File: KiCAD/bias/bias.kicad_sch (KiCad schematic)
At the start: 67 parts, among them J1 Conn_Coaxial_Small, J11 GRID_BIAS, J2 Conn_Coaxial_Small, J3 Screw_Terminal_01x02, J4 Conn_Coaxial_Small, J5 Screw_Terminal_01x02, J6 Conn_Coaxial_Small, J7 Screw_Terminal_01x02, J8 Screw_Terminal_01x02, J9 Conn_Coaxial_Small, Q2 2N7000, Q3 2N7000, U10 OPA454, U11 LM4040LP-5, U12 LM393, U13 OPA1641, U14 OPA1641, U5 OPA454, U9 LM7805_TO220

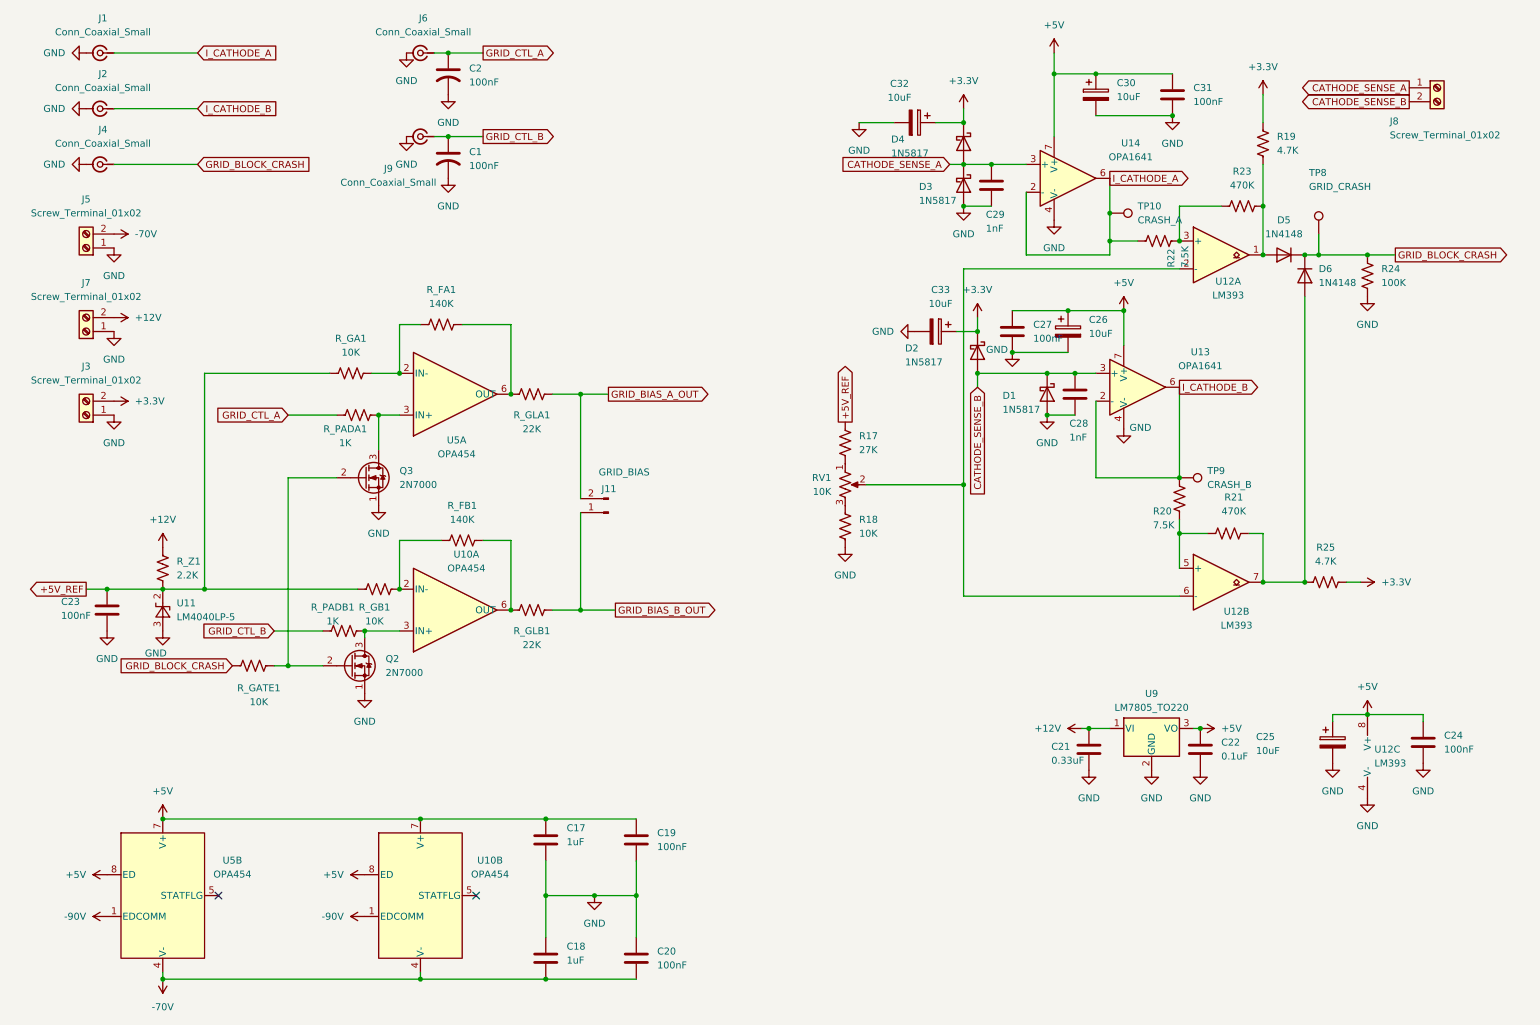
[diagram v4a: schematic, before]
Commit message: KiCad revB: schematic review pass — I2C, ENC_INT, GND returns, GRID_BLOCK_CRASH clamp
Result of extended review pass against fresh netlists across all four
boards. All connectivity blockers resolved.

- Si5351 SDA/SCL wired via 0R jumpers (R8/R9) puts I2C on PCB traces
  for PCF8575 U17 and the RJ45 to the front panel. MCP4728 side has
  parallel 0R jumpers (R3/R4/R5) left DNP by default — STEMMA-QT is
  the intended path.
- ENC_INT chain unified end-to-end with staged names:
  ENC_INT_RAW (frontpanel encoder wire-OR) → ENC_INT_CLEAN (across
  CAT + analog pass-through) → ENC_INT_FINAL (post-protoshield
  conditioning). Frontpanel U4 (MCP1700-3.3 LDO) sources the +3.3V
  the pull-up R4 needs; pull-up moved to encoder side for sharper
  falling edges over the 2 m CAT run.
- Protoshield GRID_BLOCK_CRASH gets 1N4728A Zener clamp (D5),
  matching the I_CATHODE and MBL600 5V→3.3V clamp topology.
- Protoshield MBL600 conditioning rebuilt: 1K series + 100nF filter
  + 1N4728A clamp (was 10K/20K divider + 22pF that filtered nothing
  below RF).
- PADDLE_A/B and RESET_N removed from analog board — case-mounted
  switches wire directly to protoshield.
- Protoshield J1/J6 widened to 3-pin to include GND returns for the
  case-mounted paddle and reset switches.
- Bias board reference designators reorganized functionally
  (R_FA/R_FB feedback, R_GA/R_GB gain, R_PADA/R_PADB, R_GLA/R_GLB
  grid line, R_GATE, R_Z).
- New Documentation/control_board_functional_blocks.md captures
  KeyUp/Gate 2 keying, relay assignments (J6=T/R, J7=HV primary,
  J8=HV inrush), CD14538B heartbeat watchdog, TR_SENSE interlock,
  and J13 power-migration header.
- Fresh netlists exported for all four boards.

Co-Authored-By: Claude Opus 4.7 <noreply@anthropic.com>
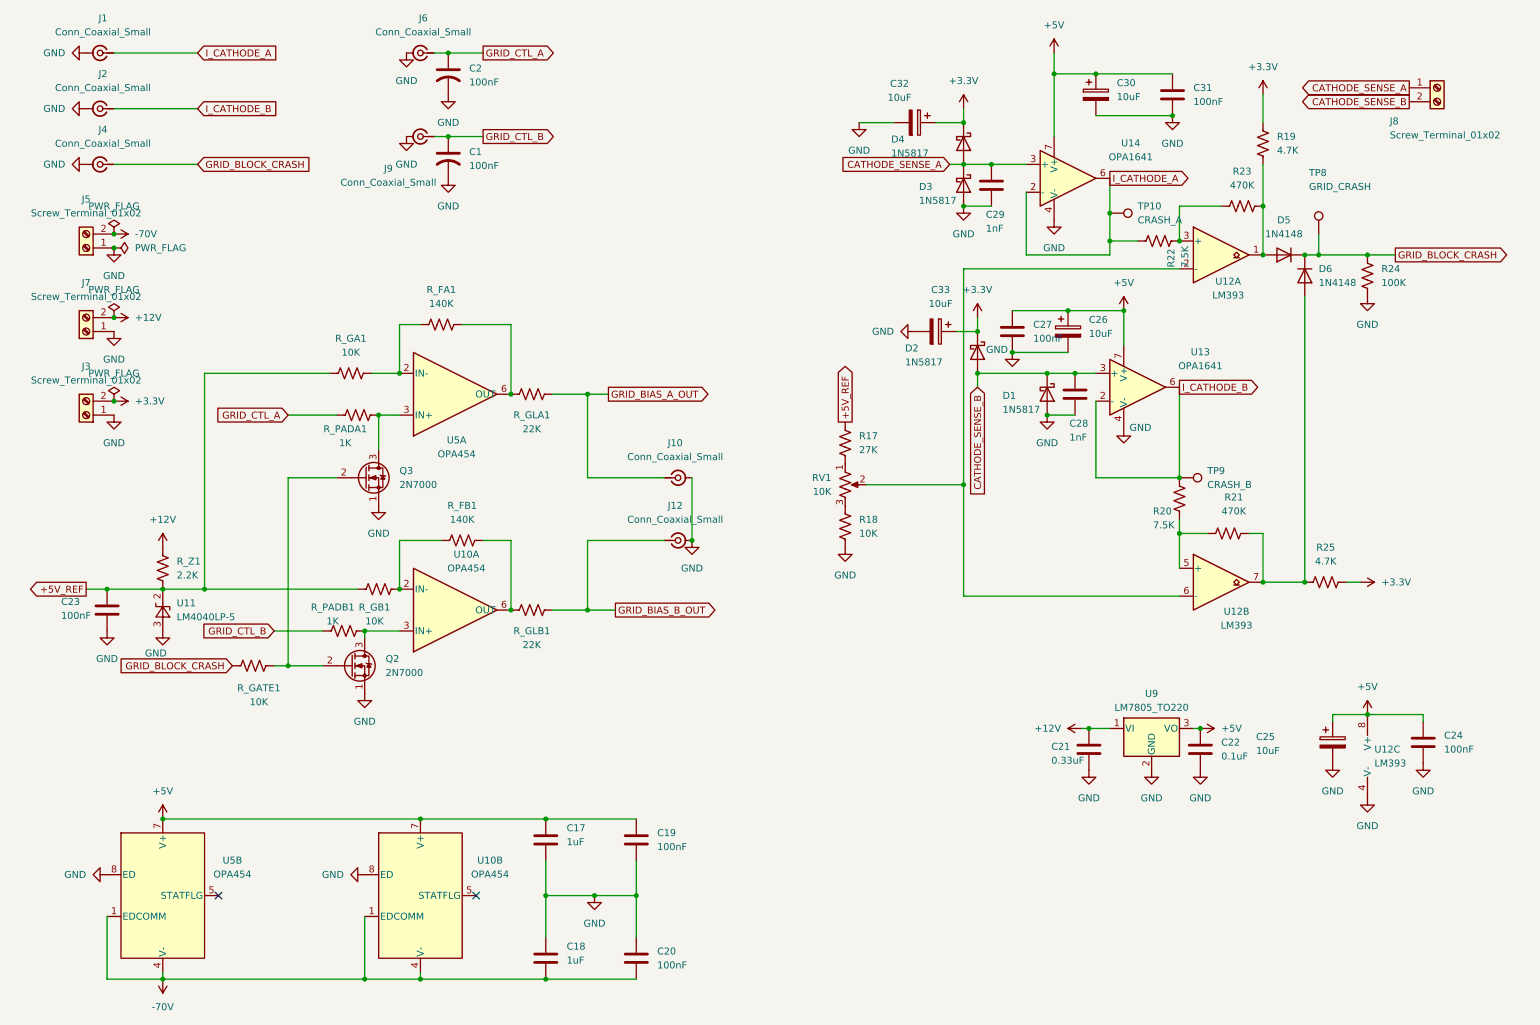
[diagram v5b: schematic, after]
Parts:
- removed J11: GRID_BIAS, Connector_PinHeader_2.54mm:PinHeader_1x02_P2.54mm_Vertical, symbol Connector:Conn_01x02_Pin
- added J10, J12: Conn_Coaxial_Small, symbol Connector:Conn_Coaxial_Small
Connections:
- net -90V is gone; now on net -70V: U10.1 (EDCOMM), U5.1 (EDCOMM)
- net +5V: no longer U10.8 (ED), U5.8 (ED)
- net GND: now also U10.8 (ED), U5.8 (ED), J10.2 (Ext), J12.2 (Ext)
- net GRID_BIAS_A_OUT: now also J10.1 (In)
- net GRID_BIAS_B_OUT: now also J12.1 (In)

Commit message: KiCad revB: assign 87 empty footprints via re-runnable scripts
Filled empty Footprint fields on capacitors, resistors, and screw
terminals across all four boards. All three scripts are re-runnable
and only fill empty fields (never overwrite existing assignments).

Scripts:
- assign_cap_footprints.py: extended CAP_LIB_IDS to also cover
  Device:C_US, Device:C_Polarized_US, Device:C_Small (was only
  Device:C and Device:C_Polarized). VALUE_TO_FOOTPRINT map unchanged.
- assign_connector_footprints.py (new): matches
  Connector:Screw_Terminal_01xNN to Phoenix MKDS-1,5-N horizontal
  P5.00mm per pin count (same pattern the protoshield already used).
- assign_resistor_footprints.py (new): matches Device:R and
  Device:R_US to the project-standard Resistor_THT:R_Axial_DIN0207
  L6.3mm_D2.5mm_P10.16mm_Horizontal footprint. All 46 populated
  resistors on the project already used this footprint; the empty
  ones now match.

Assignment counts:
- Capacitors: 42 (5 arduino, 33 vfo_complete, 2 bias, 2 frontpanel)
- Screw terminals: 17 (10 arduino, 4 bias, 1 frontpanel, 2 protoshield)
- Resistors: 28 (5 arduino, 21 vfo_complete, 2 frontpanel)

Deferred (need part-specific decisions, tracked in review notes):
- Coax connectors (12 total across analog + bias) - awaiting Cinch
  142-0701-201 footprint verification in KiCad's Connector_Coaxial
  library, or a custom footprint in xmitter.pretty/
- One-off ICs: F1 Polyfuse, U3 MCP4728, U21 LT1054
- 6 unmapped cap values in vfo_complete: 2pF x3, 220nF, 4700uF, 100uF
- U2 Metro_ESP32S3 (protoshield): intentionally empty (on_board no,
  plug-in module, not placed on PCB)

Also add three component datasheets: 1N4736AT-D (1N4728A family
reference), LM393-D, OPA1641.

Co-Authored-By: Claude Opus 4.7 <noreply@anthropic.com>
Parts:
- C1, C2: footprint (none) -> Capacitor_THT:C_Disc_D5.0mm_W2.5mm_P5.00mm
- J3, J5, J7, J8: footprint (none) -> TerminalBlock_Phoenix:TerminalBlock_Phoenix_MKDS-1,5-2_1x02_P5.00mm_Horizontal
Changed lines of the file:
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@@
 			)
 		)
-		(property "Footprint" ""
+		(property "Footprint" "TerminalBlock_Phoenix:TerminalBlock_Phoenix_MKDS-1,5-2_1x02_P5.00mm_Horizontal"
 			(at 24.13 71.12 0)
 			(hide yes)
@@
 			)
 		)
-		(property "Footprint" ""
+		(property "Footprint" "TerminalBlock_Phoenix:TerminalBlock_Phoenix_MKDS-1,5-2_1x02_P5.00mm_Horizontal"
 			(at 270.51 26.67 0)
 			(hide yes)
@@
 			)
 		)
-		(property "Footprint" ""
+		(property "Footprint" "Capacitor_THT:C_Disc_D5.0mm_W2.5mm_P5.00mm"
 			(at 90.17 39.37 0)
 			(hide yes)
@@
 			)
 		)
-		(property "Footprint" ""
+		(property "Footprint" "TerminalBlock_Phoenix:TerminalBlock_Phoenix_MKDS-1,5-2_1x02_P5.00mm_Horizontal"
 			(at 24.13 86.36 0)
 			(hide yes)
@@
 			)
 		)
-		(property "Footprint" ""
+		(property "Footprint" "Capacitor_THT:C_Disc_D5.0mm_W2.5mm_P5.00mm"
 			(at 90.17 24.13 0)
 			(hide yes)
@@
 			)
 		)
-		(property "Footprint" ""
+		(property "Footprint" "TerminalBlock_Phoenix:TerminalBlock_Phoenix_MKDS-1,5-2_1x02_P5.00mm_Horizontal"
 			(at 24.13 55.88 0)
 			(hide yes)

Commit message: KiCad revB: custom footprints, coax assignments, TO-92 widening, ENC_INT rewire
Second-pass footprint work: filled the remaining empty footprints
that couldn't be handled by the earlier stock-library scripts, added
custom footprints for parts KiCad's stock library doesn't cover, and
did a few schematic hygiene fixes surfaced during the deep-dive
reviews.

Custom footprints (new, xmitter.pretty/):
- SMA_Cinch_142-0701-201_Vertical_JackPCB - 50 Ohm SMA vertical
  through-hole jack for the analog board and bias board coax
  interconnects (I_CATHODE, GRID_CTL, GRID_BLOCK_CRASH, GRID_BIAS).
  Center pin 1.57 mm hole + 4 ground tabs on a 5.08 mm square
  pattern. All 4 ground tabs share pin number 2 (shield).
- CP_Radial_Kemet_ESK_D22.0mm_P10.00mm - Kemet ESK case Q4 radial
  electrolytic (22 mm dia, 10 mm pitch) for C72 = 4700 uF 50V.
- Fuse_Littelfuse_60R_L7.9mm_W3.1mm_P5.08mm - Littelfuse 60R Series
  radial polyfuse for F1 = 60R050XU (0.5 A hold). Body sized for the
  small-body variants (010X-090X); pitch 5.08 mm, drill 0.7 mm.
- C_Axial_Kemet_Aximax_C41X_L4.5mm_D2.6mm_P7.62mm_Horizontal - Kemet
  Aximax C410 axial C0G ceramic for the three 2 pF caps
  (C69/C70/C71) in the vfo_complete keyer chain. Horizontal mount,
  7.62 mm pitch.

New re-runnable script:
- tools/assign_coax_footprints.py - maps
  Connector:Conn_Coaxial_Small symbols to the new Cinch SMA
  footprint. Same "only fill empty, never overwrite" pattern as the
  existing assign_*_footprints.py scripts.

Script extension:
- tools/assign_cap_footprints.py - added value entries for 4700uF
  (Kemet ESK), 220nF (D6 disc), 2pF (Kemet Aximax C41X), and 100uF
  (Vishay 036 RSP). All four entries include the datasheet path and
  the specific case-size rationale.

Schematic edits (all boards):
- 12 coax connectors assigned to the new Cinch SMA footprint
  (analog J17-J19/J23-J24, bias J1/J2/J4/J6/J9/J10/J12) via the new
  assign_coax script.
- 5 caps in vfo_complete assigned via extended assign_cap_footprints
  (C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
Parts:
- J1, J10, J12, J2, J4, J6, J9: footprint (none) -> xmitter:SMA_Cinch_142-0701-201_Vertical_JackPCB
- Q2, Q3, U11: footprint Package_TO_SOT_THT:TO-92_Inline -> Package_TO_SOT_THT:TO-92_Inline_Wide
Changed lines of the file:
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@@
 			)
 		)
-		(property "Footprint" "Package_TO_SOT_THT:TO-92_Inline"
+		(property "Footprint" "Package_TO_SOT_THT:TO-92_Inline_Wide"
 			(at 43.18 121.92 0)
 			(hide yes)
@@
 			)
 		)
-		(property "Footprint" "Package_TO_SOT_THT:TO-92_Inline"
+		(property "Footprint" "Package_TO_SOT_THT:TO-92_Inline_Wide"
 			(at 80.01 99.695 0)
 			(hide yes)
@@
 			)
 		)
-		(property "Footprint" ""
+		(property "Footprint" "xmitter:SMA_Cinch_142-0701-201_Vertical_JackPCB"
 			(at 132.08 109.22 0)
 			(hide yes)
@@
 			)
 		)
-		(property "Footprint" ""
+		(property "Footprint" "xmitter:SMA_Cinch_142-0701-201_Vertical_JackPCB"
 			(at 85.09 35.56 0)
 			(hide yes)
@@
 			)
 		)
-		(property "Footprint" ""
+		(property "Footprint" "xmitter:SMA_Cinch_142-0701-201_Vertical_JackPCB"
 			(at 26.67 40.64 0)
 			(hide yes)
@@
 			)
 		)
-		(property "Footprint" "Package_TO_SOT_THT:TO-92_Inline"
+		(property "Footprint" "Package_TO_SOT_THT:TO-92_Inline_Wide"
 			(at 77.47 133.985 0)
 			(hide yes)
@@
 			)
 		)
-		(property "Footprint" ""
+		(property "Footprint" "xmitter:SMA_Cinch_142-0701-201_Vertical_JackPCB"
 			(at 26.67 20.32 0)
 			(hide yes)
@@
 			)
 		)
-		(property "Footprint" ""
+		(property "Footprint" "xmitter:SMA_Cinch_142-0701-201_Vertical_JackPCB"
 			(at 85.09 20.32 0)
 			(hide yes)
@@
 			)
 		)
-		(property "Footprint" ""
+		(property "Footprint" "xmitter:SMA_Cinch_142-0701-201_Vertical_JackPCB"
 			(at 132.08 97.79 0)
 			(hide yes)
@@
 			)
 		)
-		(property "Footprint" ""
+		(property "Footprint" "xmitter:SMA_Cinch_142-0701-201_Vertical_JackPCB"
 			(at 26.67 30.48 0)
 			(hide yes)
